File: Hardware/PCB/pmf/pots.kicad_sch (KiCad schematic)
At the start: 36 parts, among them U3 TL072, U4 TL072

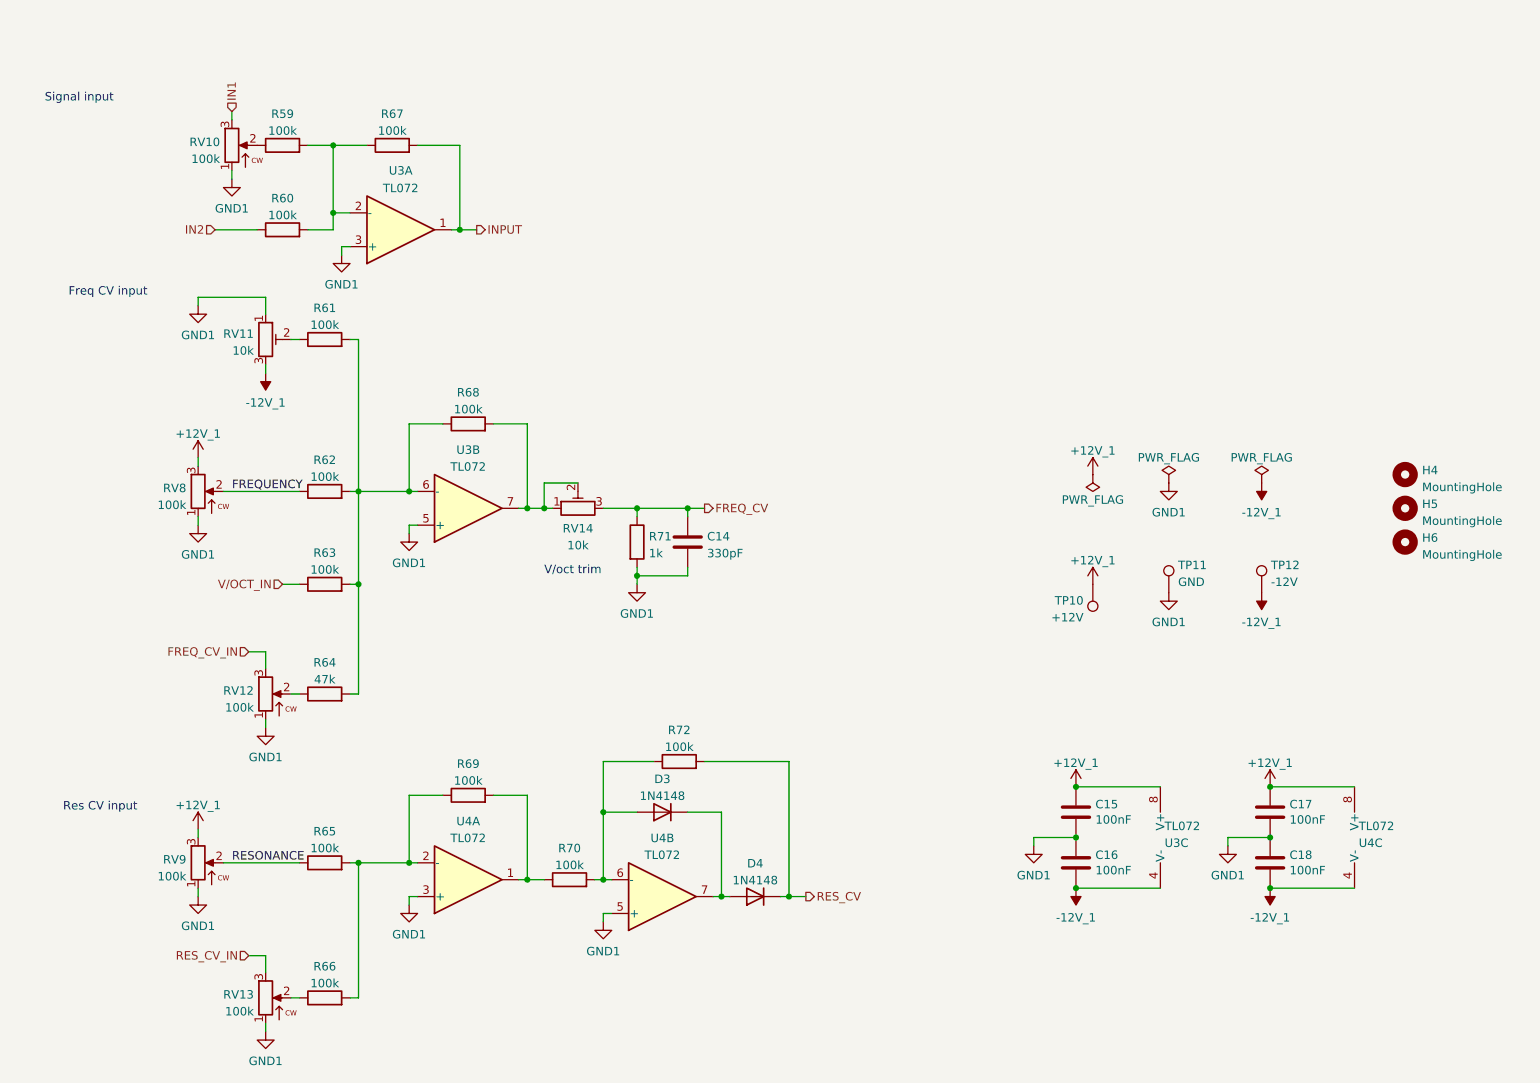
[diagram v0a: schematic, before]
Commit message: Re-invert input
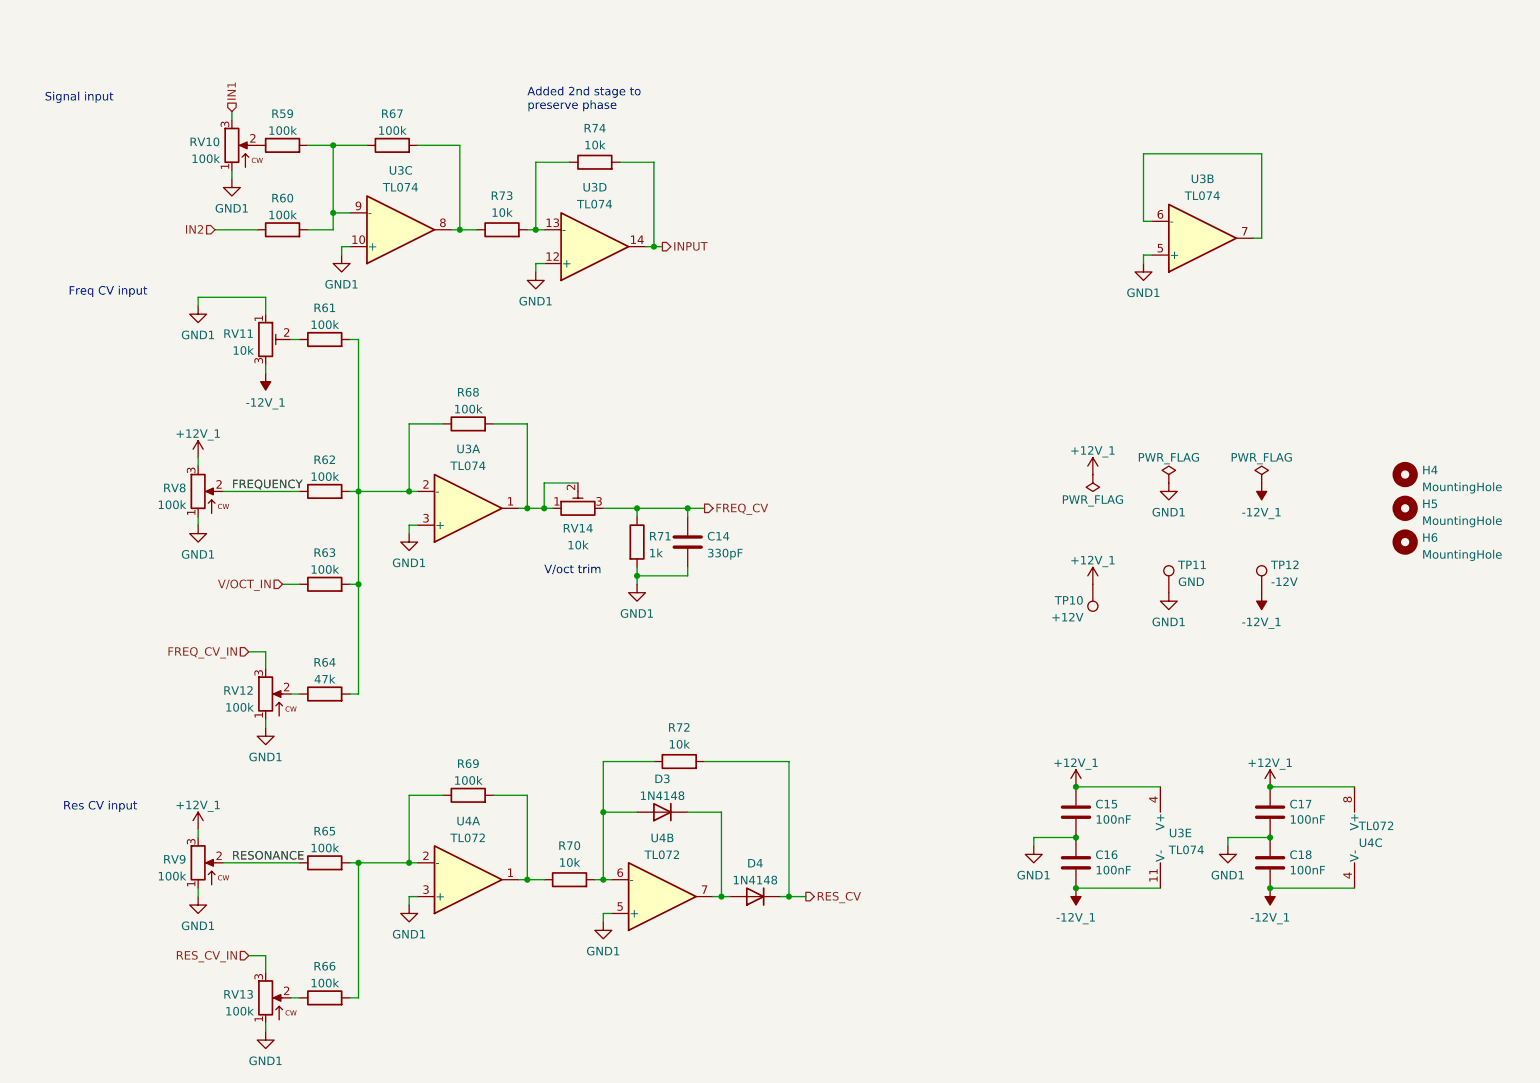
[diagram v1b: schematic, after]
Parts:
- removed U3: TL072, ao_tht:DIP-8_W7.62mm_Socket_LongPads, symbol ao_symbols:TL072
- added R73, R74: 10k, ao_tht:R_Axial_DIN0207_L6.3mm_D2.5mm_P10.16mm_Horizontal, symbol ao_symbols:R
- added U3: TL074, ao_tht:DIP-14_W7.62mm_Socket_LongPads, symbol ao_symbols:TL074
- R70, R72: value 100k -> 10k
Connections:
- net +12V_1: now also U3.4 (V+)
- net -12V_1: now also U3.11 (V-)
- net GND1: now also U3.10 (+), U3.12 (+), U3.3 (+), U3.5 (+)
- net INPUT: now also R74.2, U3.14; no longer R67.2
- net at R59.2, R60.2, R67.1: now also U3.9 (-)
- net at R61.2, R62.2, R63.2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: now also U3.2 (-)
- net at R68.2, RV14.1, RV14.2: now also U3.1
- new net: U3.6 (-), U3.7
- new net: R73.2, R74.1, U3.13 (-)
- new net: R67.2, R73.1, U3.8
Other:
- note added: "Added 2nd stage to preserve phase"

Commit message: Rename libraries
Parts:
- C14: footprint ao_tht:C_Rect_L7.2mm_W2.5mm_P5.00mm_FKS2_FKP2_MKS2_MKP2 -> AO_tht:C_Rect_L7.2mm_W2.5mm_P5.00mm_FKS2_FKP2_MKS2_MKP2; symbol ao_symbols:C -> AO_symbols:C
- C15, C16, C17, C18: footprint ao_tht:C_Disc_D3.0mm_W1.6mm_P2.50mm -> AO_tht:C_Disc_D3.0mm_W1.6mm_P2.50mm; symbol ao_symbols:C -> AO_symbols:C
- D3, D4: footprint ao_tht:D_DO-35_SOD27_P7.62mm_Horizontal -> AO_tht:D_DO-35_SOD27_P7.62mm_Horizontal; symbol ao_symbols:1N4148 -> AO_symbols:1N4148
- H4, H5, H6: footprint ao_tht:MountingHole_3.2mm_M3 -> AO_tht:MountingHole_3.2mm_M3; symbol ao_symbols:MountingHole -> AO_symbols:MountingHole
- R59, R60, R61, R62, R63, R64, R65, R66, R67, R68, R69, R70, R71, R72, R73, R74: footprint ao_tht:R_Axial_DIN0207_L6.3mm_D2.5mm_P10.16mm_Horizontal -> AO_tht:R_Axial_DIN0207_L6.3mm_D2.5mm_P10.16mm_Horizontal; symbol ao_symbols:R -> AO_symbols:R
- RV10, RV12, RV13, RV8, RV9: footprint ao_tht:Potentiometer_Alpha_16mm_Single_Vertical -> AO_tht:Potentiometer_Alpha_16mm_Single_Vertical; symbol ao_symbols:R_POT -> AO_symbols:R_POT
- RV11, RV14: symbol ao_symbols:R_POT_TRIM_3296W -> AO_symbols:R_POT_TRIM_3296W
- TP10, TP11, TP12: footprint ao_tht:TestPoint_THTPad_D1.5mm_Drill0.7mm -> AO_tht:TestPoint_THTPad_D1.5mm_Drill0.7mm; symbol ao_symbols:TestPoint -> AO_symbols:TestPoint
- U3: footprint ao_tht:DIP-14_W7.62mm_Socket_LongPads -> AO_tht:DIP-14_W7.62mm_Socket_LongPads; symbol ao_symbols:TL074 -> AO_symbols:TL074
- U4: footprint ao_tht:DIP-8_W7.62mm_Socket_LongPads -> AO_tht:DIP-8_W7.62mm_Socket_LongPads; symbol ao_symbols:TL072 -> AO_symbols:TL072

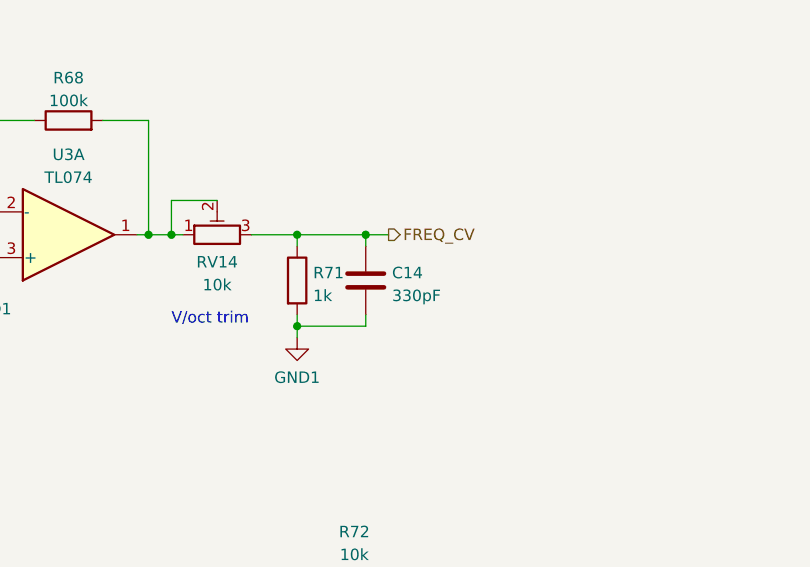
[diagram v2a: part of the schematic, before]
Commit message: Add missing resistor
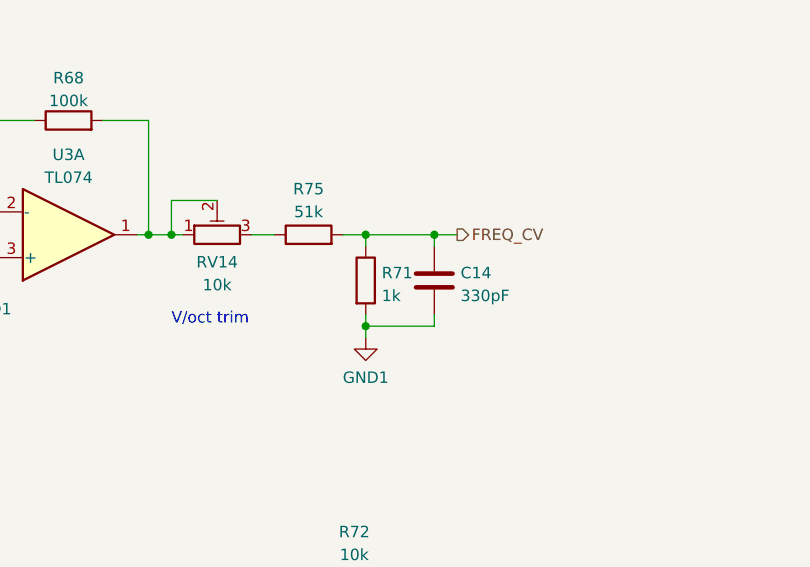
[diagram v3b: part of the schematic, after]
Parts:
- added R75: 51k, AO_tht:R_Axial_DIN0207_L6.3mm_D2.5mm_P10.16mm_Horizontal, symbol AO_symbols:R
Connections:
- net FREQ_CV: now also R75.2; no longer RV14.3
- new net: R75.1, RV14.3
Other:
- moved on the sheet: C14, R71

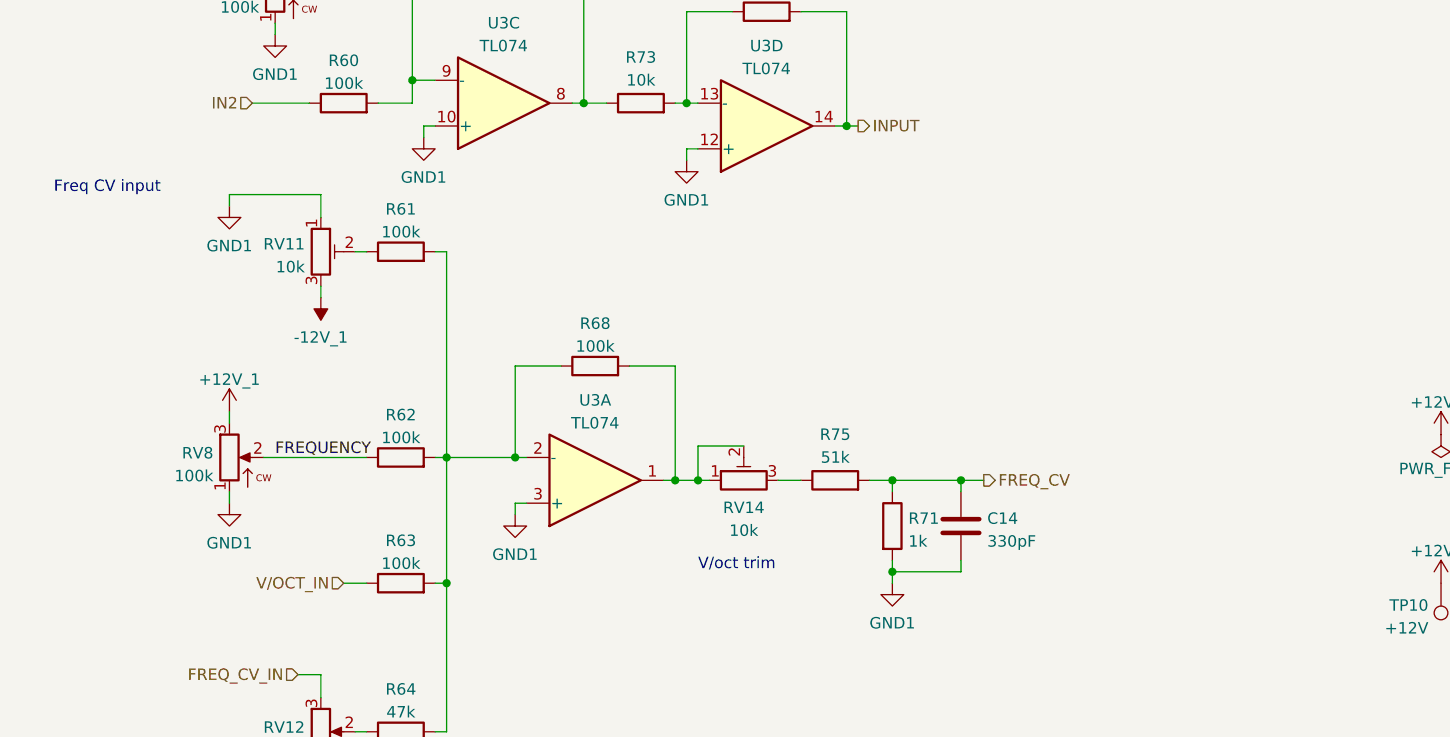
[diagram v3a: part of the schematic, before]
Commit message: Reposition pot board trimmers; ±12 V range for CV offset
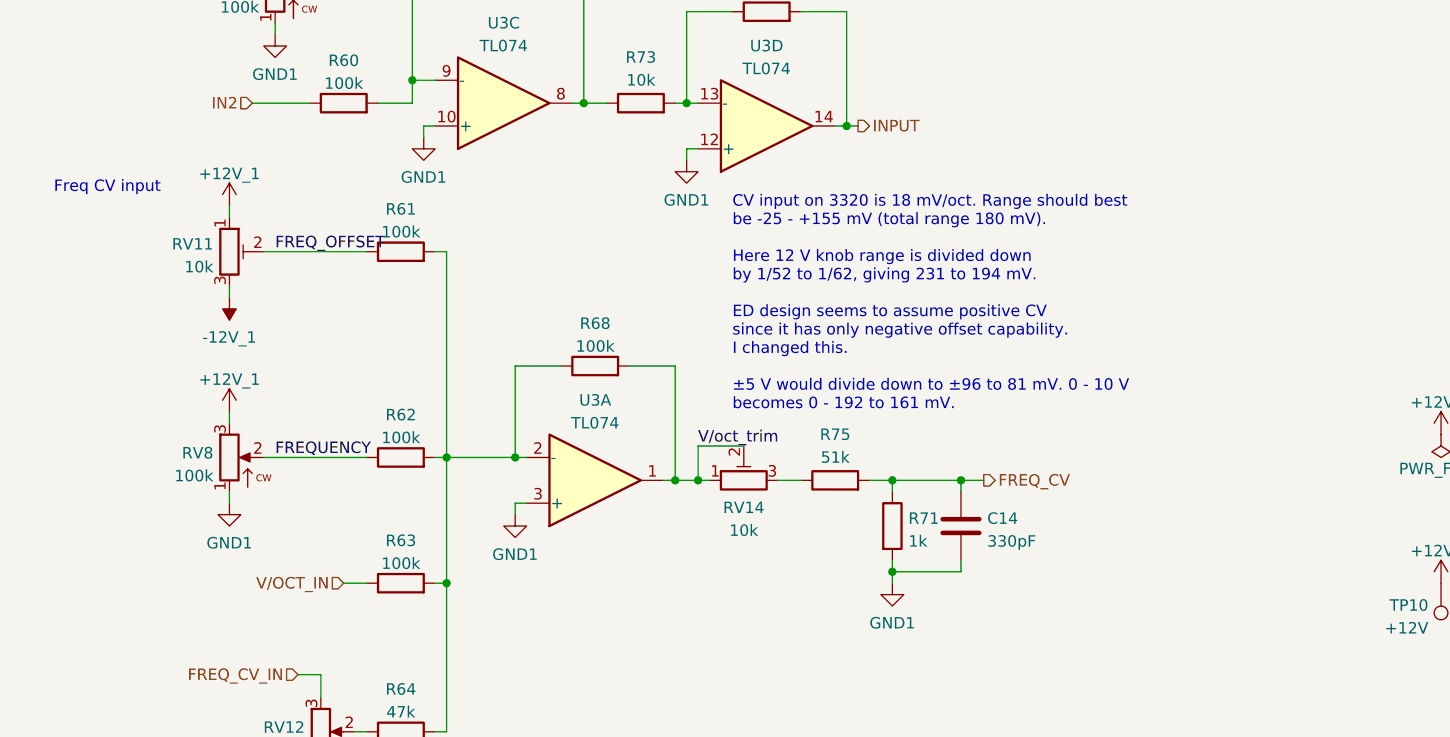
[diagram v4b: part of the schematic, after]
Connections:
- net +12V_1: now also RV11.1
- net GND1: no longer RV11.1
- net V/oct_trim: now reaches R68.2, RV14.1, RV14.2, U3.1
- net FREQ_OFFSET: now reaches R61.1, RV11.2
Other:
- note added: "CV input on 3320 is 18 mV/oct. Range should best be -25 - +155 mV (total range 180 mV). Here 12 V knob range is divided down by 1/52 to 1/62, giving 231 to 194 mV. ED design seems to assume positive CV since it has only negative offset capability. I changed this. ±5 V would divide down to ±96 to 81 mV. 0 - 10 V becomes 0 - 192 to 161 mV."
- note removed: "V/oct trim"
- moved on the sheet: RV11
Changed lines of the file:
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@@
-    (stroke (width 0) (type default))
-  )
-  (wire (pts (xy 63.5 59.69) (xy 63.5 58.42))
     (stroke (width 0) (type default))
   )
@@
     (stroke (width 0) (type default))
   )
-  (wire (pts (xy 73.66 58.42) (xy 73.66 60.96))
+  (wire (pts (xy 63.5 59.69) (xy 63.5 60.96))
     (stroke (width 0) (type default))
   )
@@
     (stroke (width 0) (type default))
   )
-  (wire (pts (xy 73.66 69.85) (xy 73.66 68.58))
+  (wire (pts (xy 63.5 69.85) (xy 63.5 68.58))
     (stroke (width 0) (type default))
   )
@@
     (stroke (width 0) (type default))
   )
-  (wire (pts (xy 77.47 64.77) (xy 78.74 64.77))
+  (wire (pts (xy 67.31 64.77) (xy 78.74 64.77))
     (stroke (width 0) (type default))
   )
@@
   )
   (wire (pts (xy 132.08 128.27) (xy 124.46 128.27))
-    (stroke (width 0) (type default))
-  )
-  (wire (pts (xy 63.5 58.42) (xy 73.66 58.42))
     (stroke (width 0) (type default))
   )
@@
     (effects (font (size 1.27 1.27)) (justify left bottom))
   )
+  (text "CV input on 3320 is 18 mV/oct. Range should best \nbe -25 - +155 mV (total range 180 mV).\n\nHere 12 V knob range is divided down \nby 1/52 to 1/62, giving 231 to 194 mV.\n\nED design seems to assume positive CV \nsince it has only negative offset capability.\nI changed this.\n\n±5 V would divide down to ±96 to 81 mV. 0 - 10 V\nbecomes 0 - 192 to 161 mV."
+    (at 119.38 82.55 0)
+    (effects (font (size 1.27 1.27)) (justify left bottom))
+  )
   (text "Signal input" (at 50.8 29.21 0)
     (effects (font (size 1.27 1.27)) (justify right bottom))
@@
     (effects (font (size 1.27 1.27)) (justify left bottom))
   )
-  (text "V/oct trim" (at 115.57 100.33 0)
+  (label "FREQUENCY" (at 68.58 87.63 0) (fields_autoplaced)
     (effects (font (size 1.27 1.27)) (justify left bottom))
   )
-  (label "FREQUENCY" (at 68.58 87.63 0) (fields_autoplaced)
+  (label "FREQ_OFFSET" (at 68.58 64.77 0) (fields_autoplaced)
+    (effects (font (size 1.27 1.27)) (justify left bottom))
+  )
+  (label "V{slash}oct_trim" (at 115.57 86.36 0) (fields_autoplaced)
     (effects (font (size 1.27 1.27)) (justify left bottom))
   )
@@
     )
   )
+  (symbol (lib_id "AO_symbols:+12V_1") (at 63.5 59.69 0) (unit 1)
+    (in_bom yes) (on_board yes) (dnp no) (fields_autoplaced)
+    (property "Reference" "#PWR076" (at 63.5 63.5 0)
+      (effects (font (size 1.27 1.27)) hide)
+    )
+    (property "Value" "+12V_1" (at 63.5 56.1142 0)
+      (effects (font (size 1.27 1.27)))
+    )
+    (property "Footprint" "" (at 63.5 59.69 0)
+      (effects (font (size 1.27 1.27)) hide)
+    )
+    (property "Datasheet" "" (at 63.5 59.69 0)
+      (effects (font (size 1.27 1.27)) hide)
+    )
+    (pin "1")
+    (instances
+      (project "pmf"
+        (path "/1fce46f5-2003-4c7e-915f-b9b7dfc679d7/0aa8016e-2b4e-464b-bdf9-8e797d920379"
+          (reference "#PWR076") (unit 1)
+        )
+      )
+    )
+  )
   (symbol (lib_id "AO_symbols:TestPoint") (at 198.12 101.6 0) (mirror x) (unit 1)
     (in_bom no) (on_board yes) (dnp no) (fields_autoplaced)
@@
     )
   )
-  (symbol (lib_id "power:GND1") (at 63.5 59.69 0) (unit 1)
-    (in_bom yes) (on_board yes) (dnp no) (fields_autoplaced)
-    (property "Reference" "#PWR039" (at 63.5 66.04 0)
-      (effects (font (size 1.27 1.27)) hide)
-    )
-    (property "Value" "GND1" (at 63.5 64.1334 0)
-      (effects (font (size 1.27 1.27)))
-    )
-    (property "Footprint" "" (at 63.5 59.69 0)
-      (effects (font (size 1.27 1.27)) hide)
-    )
-    (property "Datasheet" "" (at 63.5 59.69 0)
-      (effects (font (size 1.27 1.27)) hide)
-    )
-    (pin "1")
-    (instances
-      (project "pmf"
-        (path "/1fce46f5-2003-4c7e-915f-b9b7dfc679d7/0aa8016e-2b4e-464b-bdf9-8e797d920379"
-          (reference "#PWR039") (unit 1)
-        )
-      )
-    )
-  )
   (symbol (lib_id "AO_symbols:R") (at 135.89 128.27 90) (unit 1)
     (in_bom yes) (on_board yes) (dnp no) (fields_autoplaced)
@@
     )
   )
-  (symbol (lib_id "AO_symbols:-12V_1") (at 73.66 69.85 0) (mirror x) (unit 1)
-    (in_bom yes) (on_board yes) (dnp no) (fields_autoplaced)
-    (property "Reference" "#PWR045" (at 73.66 72.39 0)
-      (effects (font (size 1.27 1.27)) hide)
-    )
-    (property "Value" "-12V_1" (at 73.66 74.2934 0)
-      (effects (font (size 1.27 1.27)))
-    )
-    (property "Footprint" "" (at 73.66 69.85 0)
-      (effects (font (size 1.27 1.27)) hide)
-    )
-    (property "Datasheet" "" (at 73.66 69.85 0)
+  (symbol (lib_id "AO_symbols:-12V_1") (at 63.5 69.85 0) (mirror x) (unit 1)
+    (in_bom yes) (on_board yes) (dnp no) (fields_autoplaced)
+    (property "Reference" "#PWR045" (at 63.5 72.39 0)
+      (effects (font (size 1.27 1.27)) hide)
+    )
+    (property "Value" "-12V_1" (at 63.5 74.2934 0)
+      (effects (font (size 1.27 1.27)))
+    )
+    (property "Footprint" "" (at 63.5 69.85 0)
+      (effects (font (size 1.27 1.27)) hide)
+    )
+    (property "Datasheet" "" (at 63.5 69.85 0)
       (effects (font (size 1.27 1.27)) hide)
     )
@@
     )
   )
-  (symbol (lib_id "AO_symbols:R_POT_TRIM_3296W") (at 73.66 64.77 0) (unit 1)
-    (in_bom yes) (on_board yes) (dnp no) (fields_autoplaced)
-    (property "Reference" "RV11" (at 71.8821 63.9353 0)
+  (symbol (lib_id "AO_symbols:R_POT_TRIM_3296W") (at 63.5 64.77 0) (unit 1)
+    (in_bom yes) (on_board yes) (dnp no) (fields_autoplaced)
+    (property "Reference" "RV11" (at 61.7221 63.9353 0)
       (effects (font (size 1.27 1.27)) (justify right))
     )
-    (property "Value" "10k" (at 71.8821 66.4722 0)
+    (property "Value" "10k" (at 61.7221 66.4722 0)
       (effects (font (size 1.27 1.27)) (justify right))
     )
-    (property "Footprint" "pmf:Potentiometer_Bourns_3296X_Horizontal" (at 73.66 64.77 0)
-      (effects (font (size 1.27 1.27)) hide)
-    )
-    (property "Datasheet" "~" (at 73.66 64.77 0)
-      (effects (font (size 1.27 1.27)) hide)
-    )
-    (property "Vendor" "Tayda" (at 73.66 64.77 0)
-      (effects (font (size 1.27 1.27)) hide)
-    )
+    (property "Footprint" "pmf:Potentiometer_Bourns_3296X_Horizontal" (at 63.5 64.77 0)
+      (effects (font (size 1.27 1.27)) hide)
+    )
+    (property "Datasheet" "~" (at 63.5 64.77 0)
+      (effects (font (size 1.27 1.27)) hide)
+    )
+    (property "Vendor" "Tayda" (at 63.5 64.77 0)
+      (effects (font (size 1.27 1.27)) hide)
+    )
